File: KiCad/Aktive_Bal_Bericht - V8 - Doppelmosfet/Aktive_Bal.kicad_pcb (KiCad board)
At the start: 4 copper layers, 122 x 101.3 mm, 226 parts, among them J1 Screw_Terminal_01x02, J10 Conn_01x02_Pin, J11 Conn_01x02_Pin, J12 Conn_01x02_Pin, J13 Conn_01x02_Pin, J14 Conn_01x02_Pin, J15 Screw_Terminal_01x03, J16 Screw_Terminal_01x03, J17 Screw_Terminal_01x03, J18 Screw_Terminal_01x03, J19 Screw_Terminal_01x03, J2 A-DF_09_A_KG-T4S, J20 Screw_Terminal_01x03, J21 Conn_01x02_Pin, J22 Conn_01x02_Pin, J23 Conn_01x02_Pin, J24 Conn_01x02_Pin, J3 Conn_01x02_Pin, J4 Conn_01x02_Pin, J5 Conn_01x02_Pin, J6 Conn_01x02_Pin, J7 Sockel_BluePill, J9 Conn_01x02_Pin, Q1 BSS316NH6327XTSA1, Q10 Q_Dual_NMOS_G1S2G2D2S1D1, Q11 Q_Dual_NMOS_G1S2G2D2S1D1, Q12 Q_Dual_NMOS_G1S2G2D2S1D1, Q13 Q_Dual_NMOS_G1S2G2D2S1D1, Q14 Q_Dual_NMOS_G1S2G2D2S1D1, Q15 Q_Dual_NMOS_G1S2G2D2S1D1, Q16 Q_Dual_NMOS_G1S2G2D2S1D1, Q17 Q_Dual_NMOS_G1S2G2D2S1D1, Q18 Q_Dual_NMOS_G1S2G2D2S1D1, Q19 Q_Dual_NMOS_G1S2G2D2S1D1, Q2 Q_Dual_NMOS_G1S2G2D2S1D1, Q20 Q_Dual_NMOS_G1S2G2D2S1D1, Q21 Q_Dual_NMOS_G1S2G2D2S1D1, Q22 Q_Dual_NMOS_G1S2G2D2S1D1, Q23 Q_Dual_NMOS_G1S2G2D2S1D1, Q24 Q_Dual_NMOS_G1S2G2D2S1D1, Q25 Q_Dual_NMOS_G1S2G2D2S1D1, Q26 Q_Dual_NMOS_G1S2G2D2S1D1, Q27 Q_Dual_NMOS_G1S2G2D2S1D1, Q28 Q_Dual_NMOS_G1S2G2D2S1D1, Q29 Q_Dual_NMOS_G1S2G2D2S1D1, Q3 Q_Dual_NMOS_G1S2G2D2S1D1, Q30 Q_Dual_NMOS_G1S2G2D2S1D1, Q31 Q_Dual_NMOS_G1S2G2D2S1D1, Q32 Q_Dual_NMOS_G1S2G2D2S1D1, Q33 Q_Dual_NMOS_G1S2G2D2S1D1, Q4 Q_Dual_NMOS_G1S2G2D2S1D1, Q5 Q_Dual_NMOS_G1S2G2D2S1D1, Q6 Q_Dual_NMOS_G1S2G2D2S1D1, Q7 Q_Dual_NMOS_G1S2G2D2S1D1, Q8 Q_Dual_NMOS_G1S2G2D2S1D1, Q9 Q_Dual_NMOS_G1S2G2D2S1D1, U1 RFP12N10L, U10 LTV-847S, U11 LTV-847S, U12 LTV-847S, U13 LTV-847S, U14 TL084, U15 LM2596S-ADJ, U2 ADUM1250ARZ-RL7, U3 SN65HVD233, U4 SCW20C-12, U5 EC1SA16N, U6 PCA9306DC, U7 PCF8575CDB, U8 LM1117MP-3.3, U9 MCP4725xxx-xCH

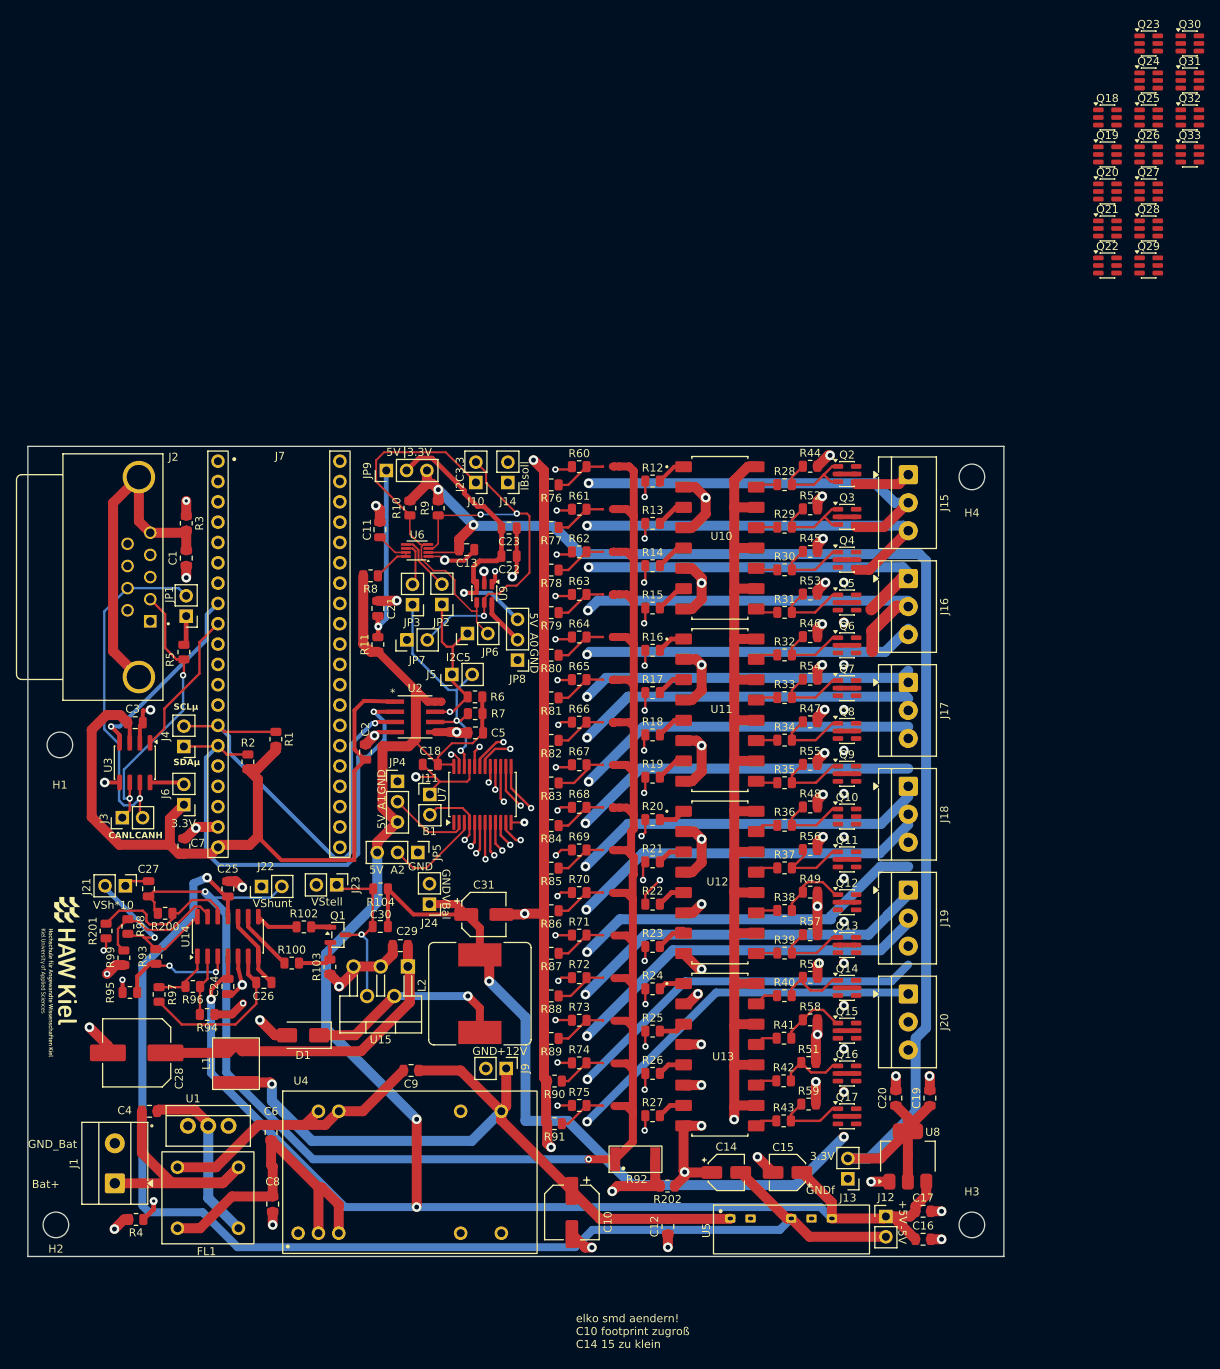
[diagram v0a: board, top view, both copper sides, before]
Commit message: mosfets verkabelt elkos getauscht
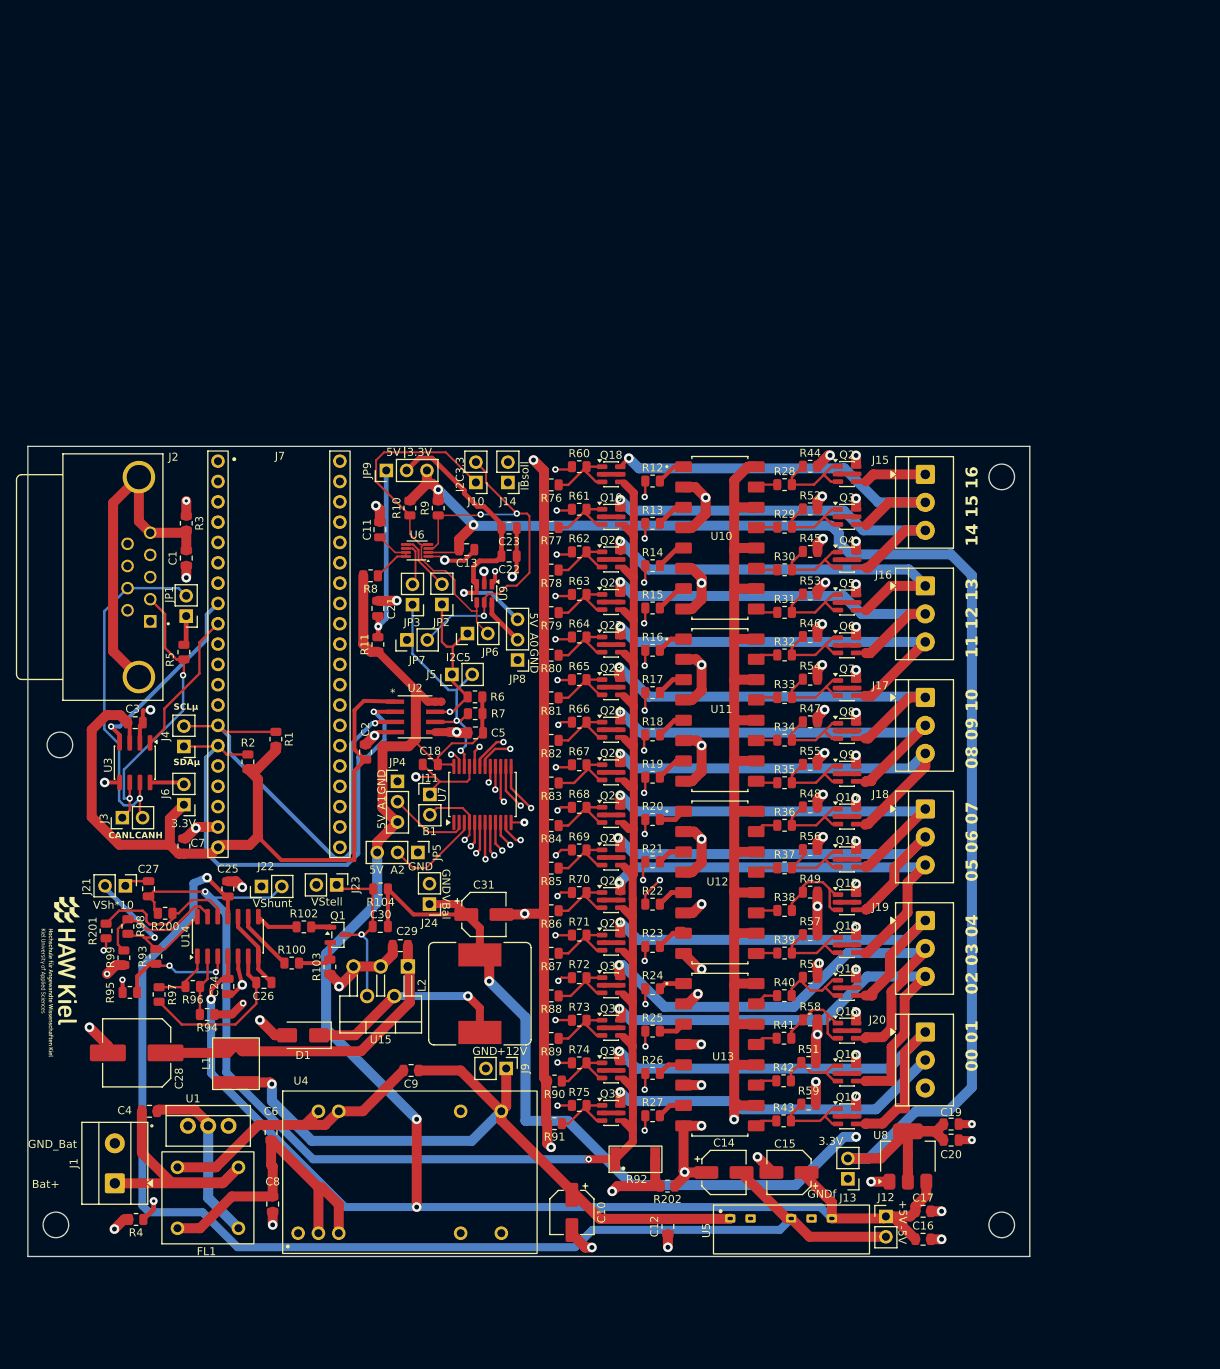
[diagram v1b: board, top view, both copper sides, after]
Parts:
- C10: footprint Capacitor_SMD:CP_Elec_6.3x5.7 -> Capacitor_SMD:CP_Elec_5x5.3
- C14, C15: footprint Capacitor_SMD:CP_Elec_4x5.4 -> Capacitor_SMD:CP_Elec_5x5.3
- moved Q33 140.0 mm to (193.9, 102.3)
- moved Q32 139.4 mm to (193.9, 97.0)
- moved Q31 138.8 mm to (193.9, 91.7)
- moved Q30 138.2 mm to (193.9, 86.3)
- moved Q29 108.1 mm to (193.9, 81.0)
- moved Q28 107.5 mm to (193.9, 75.7)
- moved Q27 107.0 mm to (193.9, 70.4)
- moved Q26 106.4 mm to (193.9, 65.1)
- moved Q25 105.9 mm to (193.9, 59.7)
- moved Q24 105.4 mm to (193.9, 54.4)
- moved Q23 104.8 mm to (193.9, 49.1)
- moved Q22 78.1 mm to (193.9, 43.8)
- moved Q21 77.6 mm to (193.9, 38.4)
- moved Q20 77.2 mm to (193.9, 33.1)
- moved Q19 76.8 mm to (193.9, 27.8)
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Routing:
- net Cell2: track 0.00 -> 60.4 mm, vias 0 -> 1
- net Cell0: track 0.00 -> 42.9 mm, vias 0 -> 1
- net Cell4: track 90.3 -> 54.3 mm, vias 2 -> 1
- net Cell1: track 92.9 -> 58.6 mm, vias 2 -> 1
- net V_Shunt_High: track 230.4 -> 207.0 mm
- net Bal: track 175.7 -> 198.4 mm, vias 15 -> 18
- net Cell3: track 46.0 -> 60.4 mm
- net +3.3V: track 183.9 -> 195.6 mm
- net Cell6: track 44.0 -> 54.8 mm
- net Cell8: track 42.8 -> 52.9 mm
- net Cell5: track 44.7 -> 54.4 mm
- net Cell10: track 41.5 -> 50.7 mm
- net Cell11: track 41.5 -> 50.2 mm
- net Cell7: track 43.2 -> 51.9 mm
- net Cell9: track 42.4 -> 51.0 mm
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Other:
- board size 122 x 101.3 mm -> 125.2 x 101.3 mm
- board text added: "00 01"
- board text added: "02 03 04"
- board text added: "05 06 07"
- board text added: "08 09 10"
- board text added: "11 12 13"
- board text added: "14 15 16"
- board text removed: "elko smd aendern! C10 footprint zugroß C14 15 zu klein"

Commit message: neuu
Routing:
- net Cell9: track 51.0 -> 52.9 mm
- net Cell10: track 50.7 -> 52.3 mm
- net Cell8: track 52.9 -> 54.1 mm
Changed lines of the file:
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@@
 		)
 		(property "Value" "RFP12N10L"
-			(at -2.04 52.6325 180)
+			(at 1.497222 1.882768 180)
 			(unlocked yes)
 			(layer "F.Fab")
@@
 	)
 	(segment
+		(start 226.033444 55.509556)
+		(end 226.044 55.499)
+		(width 0.5)
+		(layer "F.Cu")
+		(net "Cell10")
+	)
+	(segment
 		(start 233.178683 50.370985)
 		(end 231.172015 50.370985)
@@
 		(net "Cell10")
 	)
+	(segment
+		(start 224.530682 55.509556)
+		(end 226.033444 55.509556)
+		(width 0.5)
+		(layer "F.Cu")
+		(net "Cell10")
+	)
 	(via
 		(at 194.929 46.609)
@@
 	)
 	(segment
-		(start 196.1228 20.4724)
-		(end 196.1071 20.4724)
+		(start 225.709219 28.748219)
+		(end 225.79 28.829)
 		(width 0.5)
 		(layer "F.Cu")
@@
 	)
 	(segment
-		(start 225.709219 28.748219)
-		(end 225.79 28.829)
+		(start 196.1228 20.4724)
+		(end 196.1071 20.4724)
 		(width 0.5)
 		(layer "F.Cu")
@@
 	)
 	(segment
+		(start 226.396176 60.861824)
+		(end 226.425 60.833)
+		(width 0.5)
+		(layer "F.Cu")
+		(net "Cell9")
+	)
+	(segment
 		(start 226.425 60.833)
 		(end 225.79 60.833)
@@
 	)
 	(segment
+		(start 224.530682 60.861824)
+		(end 226.396176 60.861824)
+		(width 0.5)
+		(layer "F.Cu")
+		(net "Cell9")
+	)
+	(segment
 		(start 195.056 52.197)
 		(end 195.056 53.056457)
@@
 	)
 	(segment
+		(start 224.530682 66.214091)
+		(end 225.583091 66.214091)
+		(width 0.5)
+		(layer "F.Cu")
+		(net "Cell8")
+	)
+	(segment
 		(start 233.178683 59.032317)
 		(end 226.044 66.167)
@@
 		(layer "F.Cu")
 		(net "Cell8")
+	)
+	(segment
+		(start 225.583091 66.214091)
+		(end 225.663 66.294)
+		(width 0.5)
+		(layer "F.Cu")
+		(net "Cell8")

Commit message: neuu
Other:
- board text added: "NC 00 01"
- board text removed: "00 01"
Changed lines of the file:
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@@
 		)
 	)
-	(gr_text "00 01 \n"
-		(at 239.887 97.155 90)
+	(gr_text "NC 00 01 \n"
+		(at 239.887 101.554 90)
 		(layer "F.SilkS")
 		(effects
